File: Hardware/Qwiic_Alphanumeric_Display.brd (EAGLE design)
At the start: 40.6 x 27.9 mm, 46 parts, among them J4 Vertical Qwiic Connector, J5 Vertical Qwiic Connector, U2 XC9140

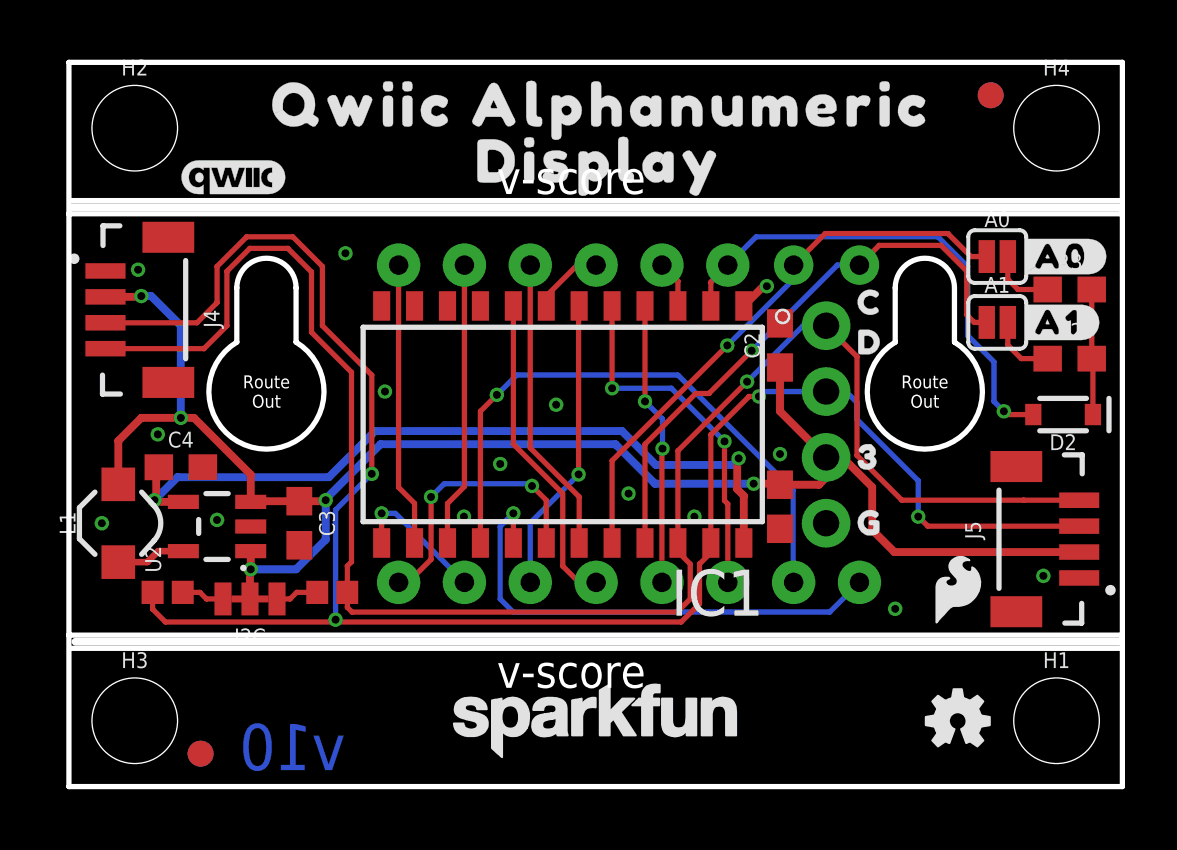
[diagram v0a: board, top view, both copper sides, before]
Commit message: QC Double-check updates
* Updated footprint of silsmart display so that pin 1 indicator was in the right place
* Moved fiducials
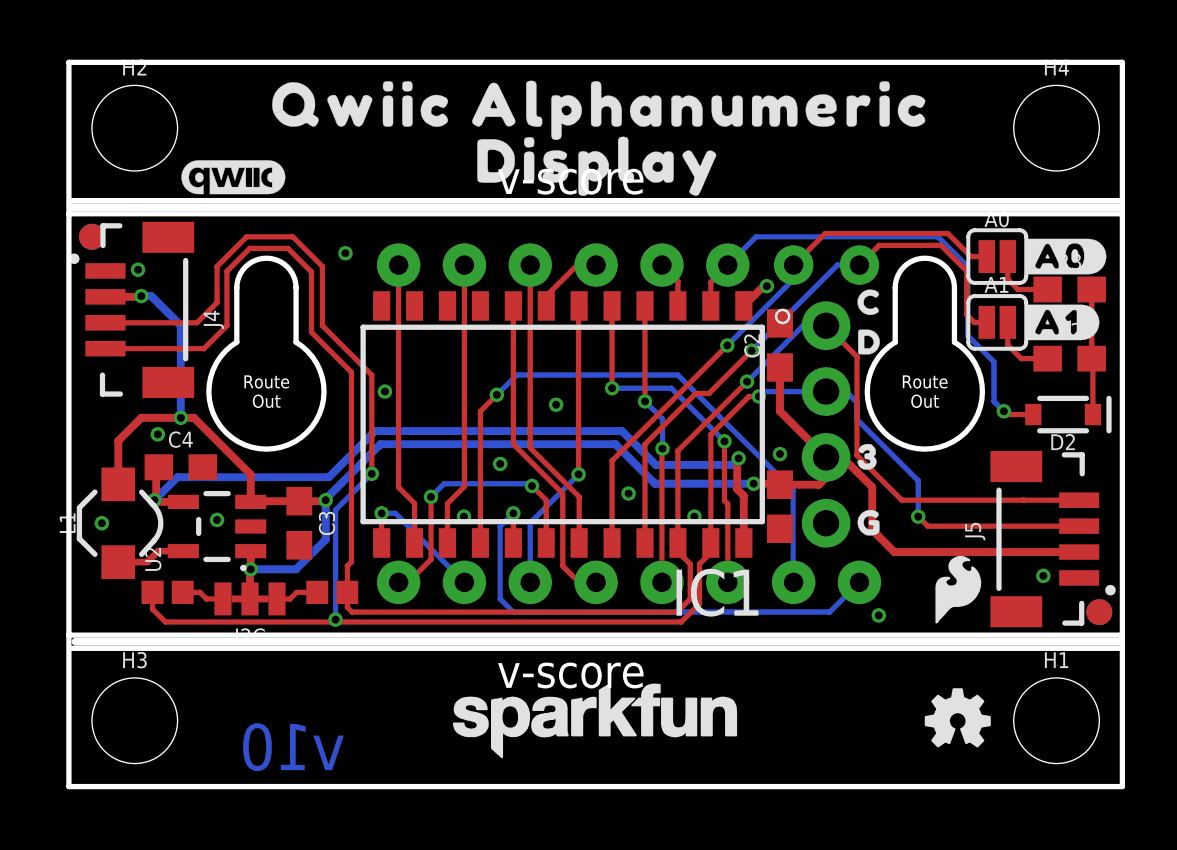
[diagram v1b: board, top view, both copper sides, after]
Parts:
- U1: value (none) -> Alphanumeric Display; device Alphanumeric_Display_Library:SILSMART_DISPLAY -> SparkFun-Displays:SILSMART_DISPLAY
- moved FD1 20.4 mm to (0.89, 21.2)
- moved FD2 20.4 mm to (0.89, 21.2)
- moved FD3 20.4 mm to (39.8, 6.73)
- moved FD4 20.4 mm to (39.8, 6.73)
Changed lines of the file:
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@@
 <layer number="154" name="FabDoc2" color="7" fill="1" visible="no" active="no"/>
 <layer number="155" name="FabDoc3" color="7" fill="1" visible="no" active="no"/>
+<layer number="156" name="gesam-Maß" color="1" fill="7" visible="no" active="no"/>
+<layer number="157" name="FaceMchng" color="3" fill="1" visible="no" active="no"/>
+<layer number="158" name="FaceMMeas" color="3" fill="1" visible="no" active="no"/>
+<layer number="159" name="Geh-Bear2" color="1" fill="7" visible="no" active="no"/>
+<layer number="160" name="Topologie" color="9" fill="1" visible="no" active="no"/>
+<layer number="161" name="tomplace2" color="7" fill="1" visible="no" active="no"/>
 <layer number="166" name="AntennaArea" color="7" fill="1" visible="no" active="no"/>
 <layer number="168" name="4mmHeightArea" color="7" fill="1" visible="no" active="no"/>
@@
 <layer number="250" name="Descript" color="3" fill="1" visible="no" active="no"/>
 <layer number="251" name="SMDround" color="12" fill="11" visible="no" active="no"/>
+<layer number="252" name="BR-BS" color="7" fill="1" visible="no" active="no"/>
 <layer number="253" name="Extra" color="7" fill="1" visible="no" active="no"/>
 <layer number="254" name="cooling" color="7" fill="1" visible="no" active="no"/>
@@
 <attribute name="VALUE" x="41.04733125" y="9.541" size="0.6096" layer="27" rot="R90"/>
 </element>
-<element name="FD1" library="SparkFun-Aesthetics" package="FIDUCIAL-1X2" value="FIDUCIAL1X2" x="5.08" y="1.27" smashed="yes"/>
-<element name="FD2" library="SparkFun-Aesthetics" package="FIDUCIAL-1X2" value="FIDUCIAL1X2" x="5.08" y="1.27" smashed="yes" rot="MR0"/>
-<element name="FD3" library="SparkFun-Aesthetics" package="FIDUCIAL-1X2" value="FIDUCIAL1X2" x="35.56" y="26.67" smashed="yes"/>
-<element name="FD4" library="SparkFun-Aesthetics" package="FIDUCIAL-1X2" value="FIDUCIAL1X2" x="35.56" y="26.67" smashed="yes" rot="MR0"/>
-<element name="U1" library="Alphanumeric_Display_Library" package="SILSMART_DISPLAY" value="" x="20.32" y="13.97" smashed="yes" rot="MR0">
+<element name="FD1" library="SparkFun-Aesthetics" package="FIDUCIAL-1X2" value="FIDUCIAL1X2" x="0.889" y="21.209" smashed="yes"/>
+<element name="FD2" library="SparkFun-Aesthetics" package="FIDUCIAL-1X2" value="FIDUCIAL1X2" x="0.889" y="21.209" smashed="yes" rot="MR0"/>
+<element name="FD3" library="SparkFun-Aesthetics" package="FIDUCIAL-1X2" value="FIDUCIAL1X2" x="39.751" y="6.731" smashed="yes"/>
+<element name="FD4" library="SparkFun-Aesthetics" package="FIDUCIAL-1X2" value="FIDUCIAL1X2" x="39.751" y="6.731" smashed="yes" rot="MR0"/>
+<element name="U1" library="SparkFun-Displays" package="SILSMART_DISPLAY" value="Alphanumeric Display" x="20.32" y="13.97" smashed="yes" rot="MR0">
 <attribute name="NAME" x="20.37" y="30.27" size="1.778" layer="26" rot="MR0"/>
 <attribute name="PROD_ID" value="COMP-14892" x="20.32" y="13.97" size="1.778" layer="28" rot="MR0" display="off"/>
-<attribute name="VALUE" x="20.42" y="11.92" size="1.778" layer="28" rot="MR0"/>
+<attribute name="VALUE" value="Alphanumeric Display" x="20.42" y="11.92" size="1.778" layer="28" rot="MR0"/>
 </element>
 <element name="H1" library="SparkFun-Hardware" package="STAND-OFF" value="STAND-OFF" x="38.1" y="2.54" smashed="yes">
@@
 <via x="27.432" y="12.827" extent="1-16" drill="0.3048"/>
 <via x="1.27" y="10.16" extent="1-16" drill="0.3048"/>
-<via x="31.877" y="6.858" extent="1-16" drill="0.3048"/>
+<via x="31.242" y="6.604" extent="1-16" drill="0.3048"/>
 <contactref element="C2" pad="2"/>
 <via x="12.192" y="15.24" extent="1-16" drill="0.3048"/>

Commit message: Change pullups from 1k to 4.7k
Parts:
- R4, R5: value 1KOHM-0402-1/16W-1% -> 4.7k; device SparkFun-Resistors:0402 -> SparkFun-Resistors:0402-TIGHT
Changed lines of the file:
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@@
 </element>
 <element name="LOGO1" library="SparkFun-Aesthetics" package="OSHW-LOGO-MINI" value="OSHW-LOGOMINI" x="34.29" y="2.54" smashed="yes"/>
-<element name="R4" library="SparkFun-Resistors" package="0402" value="1KOHM-0402-1/16W-1%" x="3.81" y="7.493" smashed="yes">
-<attribute name="PROD_ID" value="RES-14342" x="52.07" y="-57.277" size="1.778" layer="27" display="off"/>
-</element>
-<element name="R5" library="SparkFun-Resistors" package="0402" value="1KOHM-0402-1/16W-1%" x="10.16" y="7.493" smashed="yes" rot="R180">
-<attribute name="PROD_ID" value="RES-14342" x="-41.91" y="72.263" size="1.778" layer="27" rot="R180" display="off"/>
+<element name="R4" library="SparkFun-Resistors" package="0402-TIGHT" value="4.7k" x="3.81" y="7.493" smashed="yes">
+<attribute name="PROD_ID" value="RES-15343" x="52.07" y="-57.277" size="1.778" layer="27" display="off"/>
+<attribute name="VALUE" value="4.7k" x="3.81" y="7.493" size="1.778" layer="27" display="off"/>
+</element>
+<element name="R5" library="SparkFun-Resistors" package="0402-TIGHT" value="4.7k" x="10.16" y="7.493" smashed="yes" rot="R180">
+<attribute name="PROD_ID" value="RES-15343" x="-41.91" y="72.263" size="1.778" layer="27" rot="R180" display="off"/>
+<attribute name="VALUE" value="4.7k" x="10.16" y="7.493" size="1.778" layer="27" rot="R180" display="off"/>
 </element>
 <element name="A1" library="SparkFun-Jumpers" package="SMT-JUMPER_2_NO_SILK" package3d_urn="urn:adsk.eagle:package:39279/1" value="JUMPER-SMT_2_NO_SILK" x="35.814" y="17.907" smashed="yes">
@@
 <wire x1="10.287" y1="6.35" x2="3.722" y2="6.35" width="0.2032" layer="1"/>
 <wire x1="3.722" y1="6.35" x2="3.23" y2="6.842" width="0.2032" layer="1"/>
-<wire x1="3.23" y1="7.493" x2="3.23" y2="6.842" width="0.2032" layer="1"/>
+<wire x1="3.31" y1="7.493" x2="3.23" y2="6.842" width="0.2032" layer="1"/>
 <wire x1="26.2382" y1="15.0507125" x2="26.6192" y2="15.0507125" width="0.2032" layer="1"/>
 <wire x1="26.2382" y1="15.0507125" x2="24.765" y2="13.5775125" width="0.2032" layer="1"/>
@@
 <wire x1="10.9025" y1="15.9825" x2="10.9025" y2="8.6715" width="0.2032" layer="1"/>
 <wire x1="10.9025" y1="8.6715" x2="10.74" y2="8.509" width="0.2032" layer="1"/>
-<wire x1="10.74" y1="8.509" x2="10.74" y2="7.493" width="0.2032" layer="1"/>
+<wire x1="10.74" y1="8.509" x2="10.66" y2="7.493" width="0.2032" layer="1"/>
 <wire x1="10.922" y1="6.731" x2="10.74" y2="6.913" width="0.2032" layer="1"/>
-<wire x1="10.74" y1="6.913" x2="10.74" y2="7.493" width="0.2032" layer="1"/>
+<wire x1="10.74" y1="6.913" x2="10.66" y2="7.493" width="0.2032" layer="1"/>
 </signal>
 <signal name="DIG_1A">
@@
 <wire x1="5.9436" y1="7.239" x2="5.3086" y2="7.239" width="0.2032" layer="1"/>
 <wire x1="5.3086" y1="7.239" x2="5.0546" y2="7.493" width="0.2032" layer="1"/>
-<wire x1="5.0546" y1="7.493" x2="4.39" y2="7.493" width="0.2032" layer="1"/>
+<wire x1="5.0546" y1="7.493" x2="4.31" y2="7.493" width="0.2032" layer="1"/>
 </signal>
 <signal name="N$4">
@@
 <wire x1="8.0264" y1="7.239" x2="8.5344" y2="7.239" width="0.2032" layer="1"/>
 <wire x1="8.7884" y1="7.493" x2="8.5344" y2="7.239" width="0.2032" layer="1"/>
-<wire x1="8.7884" y1="7.493" x2="9.58" y2="7.493" width="0.2032" layer="1"/>
+<wire x1="8.7884" y1="7.493" x2="9.66" y2="7.493" width="0.2032" layer="1"/>
 </signal>
 </signals>

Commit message: Update Qwiic_Alphanumeric_Display.brd
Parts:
- moved R5 0.51 mm to (10.2, 8.00)
- moved R4 0.13 mm to (3.94, 7.49)
